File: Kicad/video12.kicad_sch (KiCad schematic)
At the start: 19 parts, among them J301 DE15HD, U301 THS7316, U302 TPD7S019

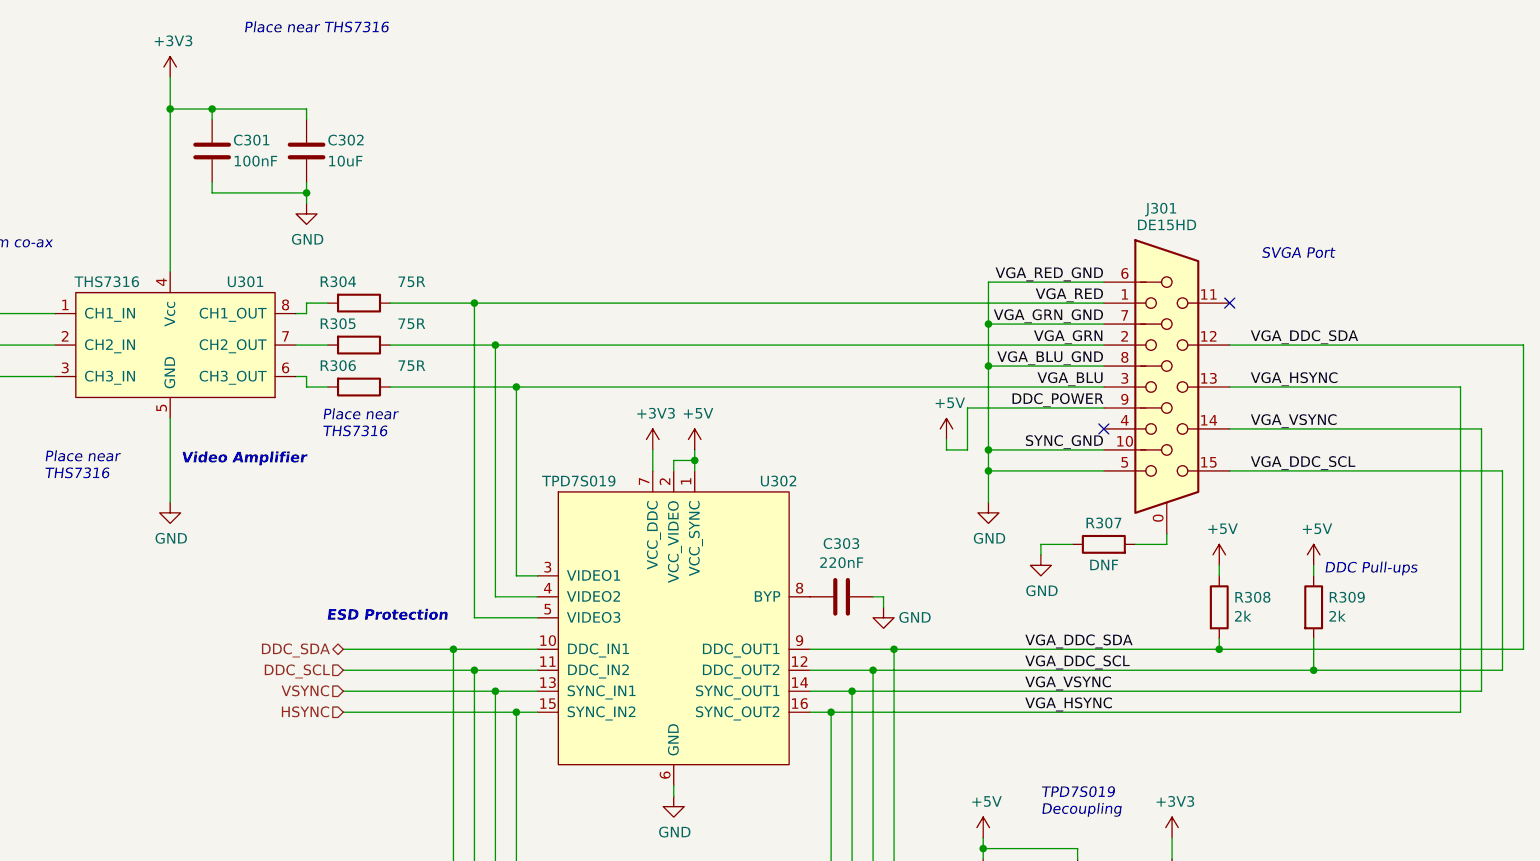
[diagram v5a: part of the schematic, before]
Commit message: LED and Switch updates.
Case LEDs are now driven by VDC and 1K. Allows higher Vf LEDs to work.
Added 6mm buttons.
Fiddled with tracking around CODEC.
Change I2S pin ordering.

Closes: #42 #60 #46
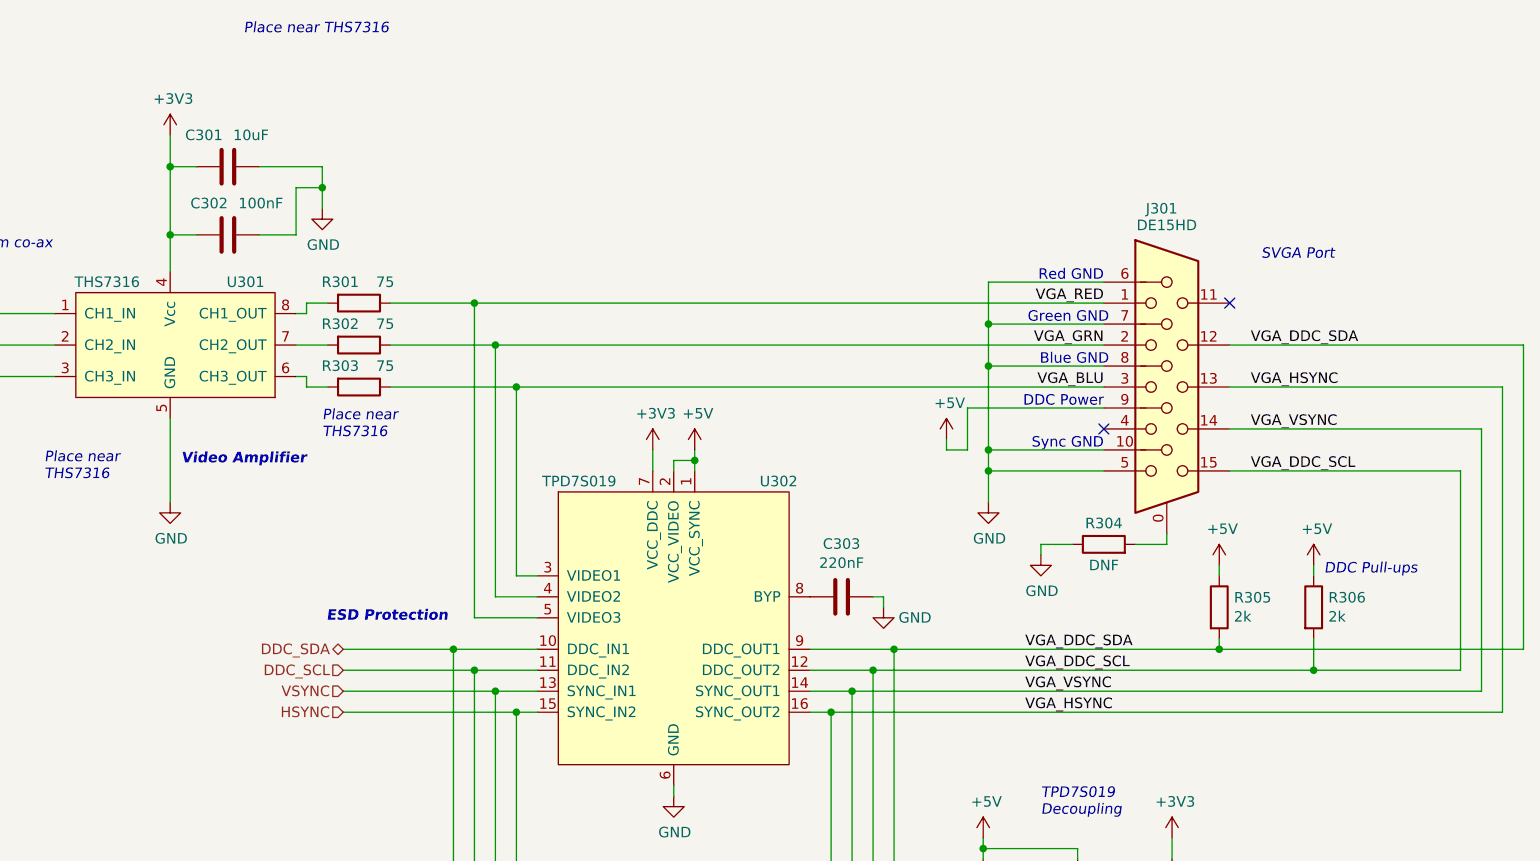
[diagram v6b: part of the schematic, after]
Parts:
- R301: renamed from R304; value 75R -> 75
- R302: renamed from R305; value 75R -> 75
- R303: renamed from R306; value 75R -> 75
- renumbered C302 to C301, C301 to C302, R307 to R304, R308 to R305, R309 to R306
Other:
- note added: "Blue GND"
- note added: "DDC Power"
- note added: "Green GND"
- note added: "Red GND"
- note added: "Sync GND"
- moved on the sheet: C301, C302

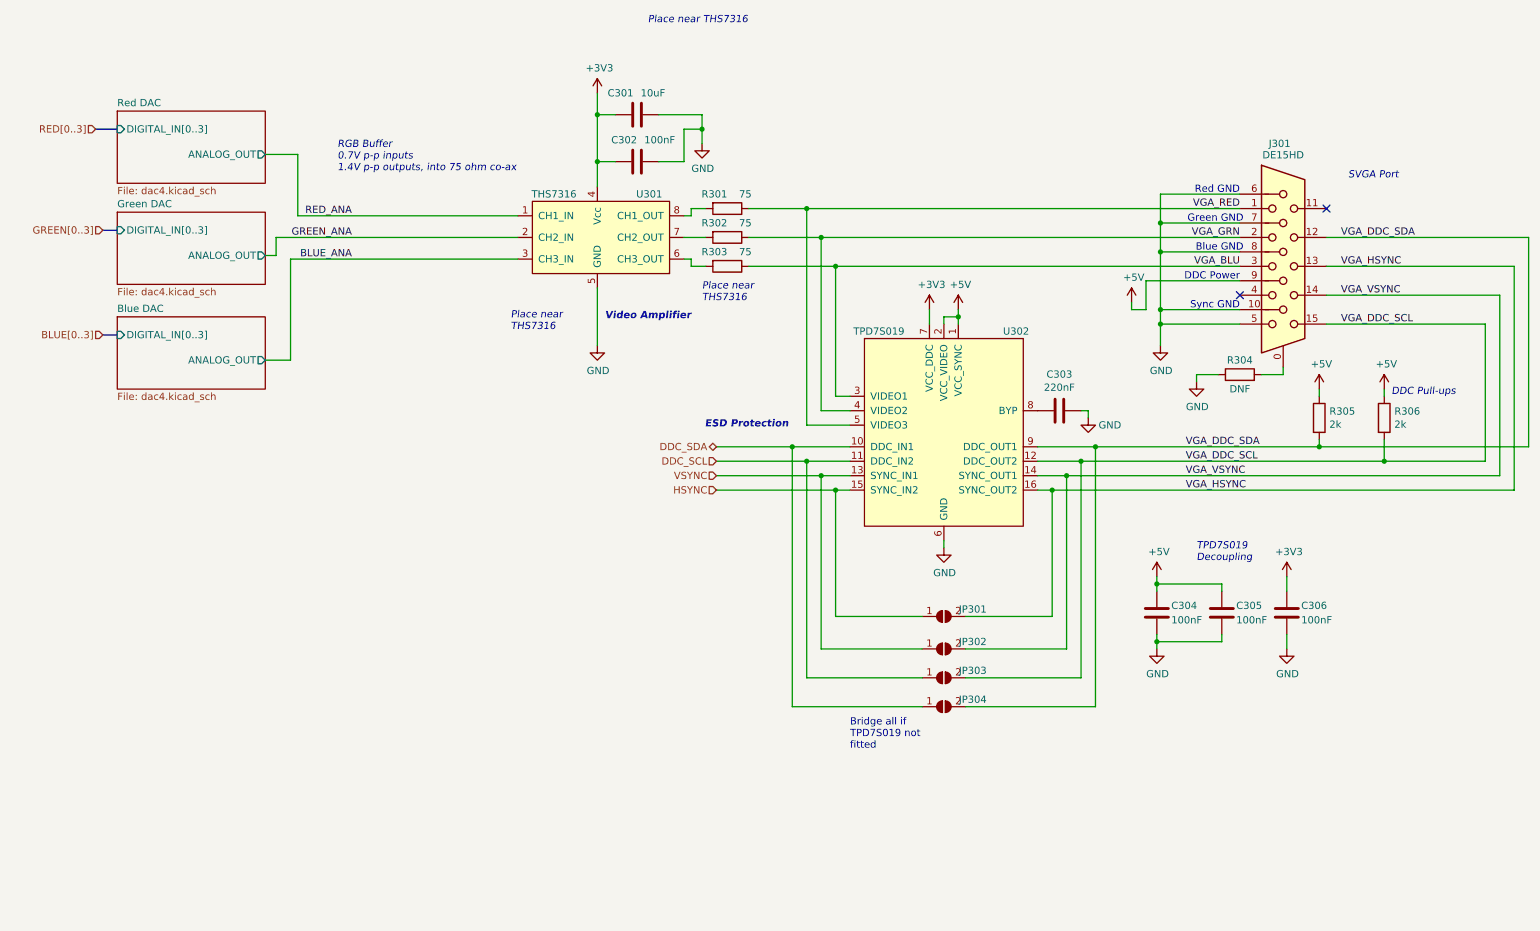
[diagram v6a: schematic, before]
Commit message: Re-organised top sheet.
Lots of parts just changed their component designator. I had
to patch up the PCB manually, but now it imports from the schematic
OK.

Also adds two PSU rails for the RTC (so you can pick DS1307
which is a 5V part, or MCP7940N which is a 3.3V part).
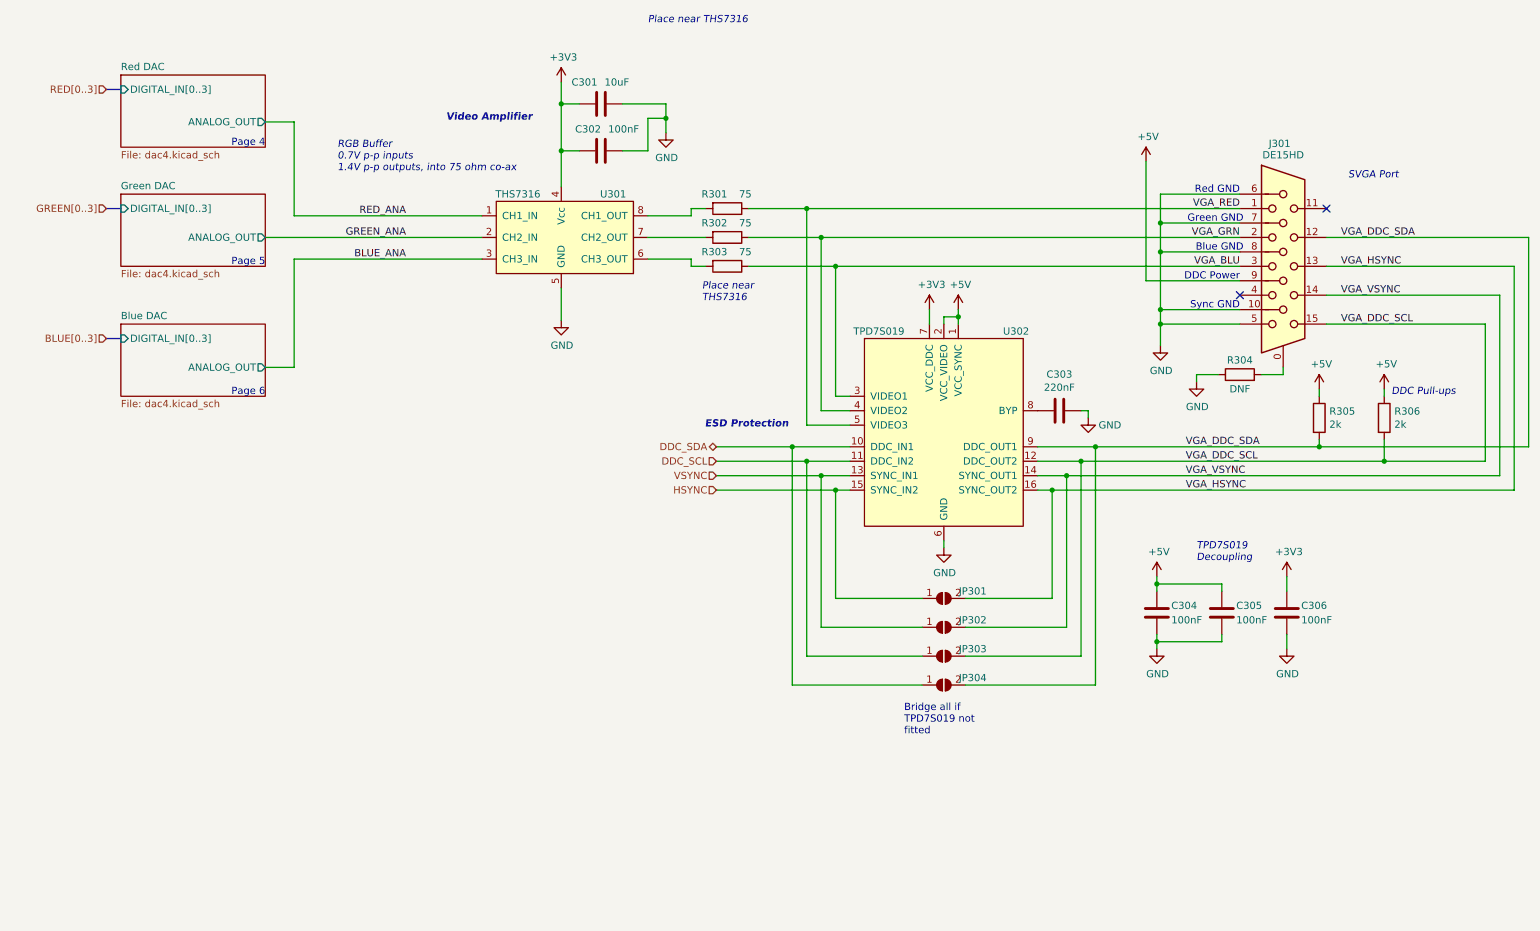
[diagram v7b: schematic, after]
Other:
- note added: "Page 4"
- note added: "Page 5"
- note added: "Page 6"
- moved on the sheet: C301, C302, JP301, JP302, JP303, JP304, U301

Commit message: Change stackup.
Top layer is now 3.3V pour + signals
Middle layers are now ground.
Bottom layer is now 5.0V pour + signals

Setting both middle layers to ground means every signal
gets a high quality return path, reducing loop area and
hopefully reducing EMI.
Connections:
- net VGA_HSYNC renamed VGA_HSYNC_BUF
- net VGA_VSYNC renamed VGA_VSYNC_BUF
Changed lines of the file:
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@@
     (effects (font (size 1.27 1.27)) (justify right bottom))
   )
-  (label "VGA_HSYNC" (at 247.65 78.74 0)
+  (label "VGA_HSYNC_BUF" (at 247.65 78.74 0)
     (effects (font (size 1.27 1.27)) (justify left bottom))
   )
@@
     (effects (font (size 1.27 1.27)) (justify right bottom))
   )
-  (label "VGA_VSYNC" (at 220.345 115.57 0)
+  (label "VGA_VSYNC_BUF" (at 220.345 115.57 0)
     (effects (font (size 1.27 1.27)) (justify left bottom))
   )
@@
     (effects (font (size 1.27 1.27)) (justify left bottom))
   )
-  (label "VGA_VSYNC" (at 247.65 83.82 0)
+  (label "VGA_VSYNC_BUF" (at 247.65 83.82 0)
     (effects (font (size 1.27 1.27)) (justify left bottom))
   )
@@
     (effects (font (size 1.27 1.27)) (justify left bottom))
   )
-  (label "VGA_HSYNC" (at 220.345 118.11 0)
+  (label "VGA_HSYNC_BUF" (at 220.345 118.11 0)
     (effects (font (size 1.27 1.27)) (justify left bottom))
   )
